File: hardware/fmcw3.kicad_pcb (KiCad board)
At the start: 4 copper layers, 101.8 x 46.8 mm, 430 parts, among them CON1 SD_Card_DM3BT, CON2 BARREL_JACK, P1 SMA, P10 CONN_01X01, P11 CONN_01X01, P12 CONN_01X01, P13 CONN_01X01, P14 CONN_01X01, P15 CONN_01X01, P16 CONN_01X01, P2 SMA, P3 CONN_02X04, P4 CONN_02X04, P5 CONN_01X01, P6 CONN_01X01, P7 CONN_01X01, P8 CONN_01X01, P9 CONN_01X01, Q1 RE1C002UN, Q2 DNP(RE1C002UN), SW1 DNP, SW2 SW_PUSH, U1 ADF4158, U10 HMC431LP4, U11 SKY65404, U12 PAT1220-6dB, U13 TRF37A73, U14 MGA-25203, U15 SMA, U16 SKY65404, U17 L7980, U18 L7980, U19 L7980, U2 LP5907-1.8, U20 LP5907-3.0, U21 LP2985A-10DBVR, U22 TPS7A91, U23 TPS7A91, U24 TPS7A91, U25 MIC5301-3.3, U26 5400BL15B050E, U27 5400BL15B050E, U28 5400BL15B050E, U29 ADL5802, U3 PAT1220-6dB, U30 XC7A15T-1FTG256C, U31 USB-MICRO, U32 93LC46B, U33 FT2232H, U34 ADA4940-2, U35 ADA4940-2, U39 LP5907-3.0, U4 KT2520K, U40 W25Q32JV, U5 NC7S04P5X, U6 NB3N551, U7 TLV172DCK, U8 LTC2292, U9 TRF37A73, Y1 ABM10-167-12.000MHZ-T3

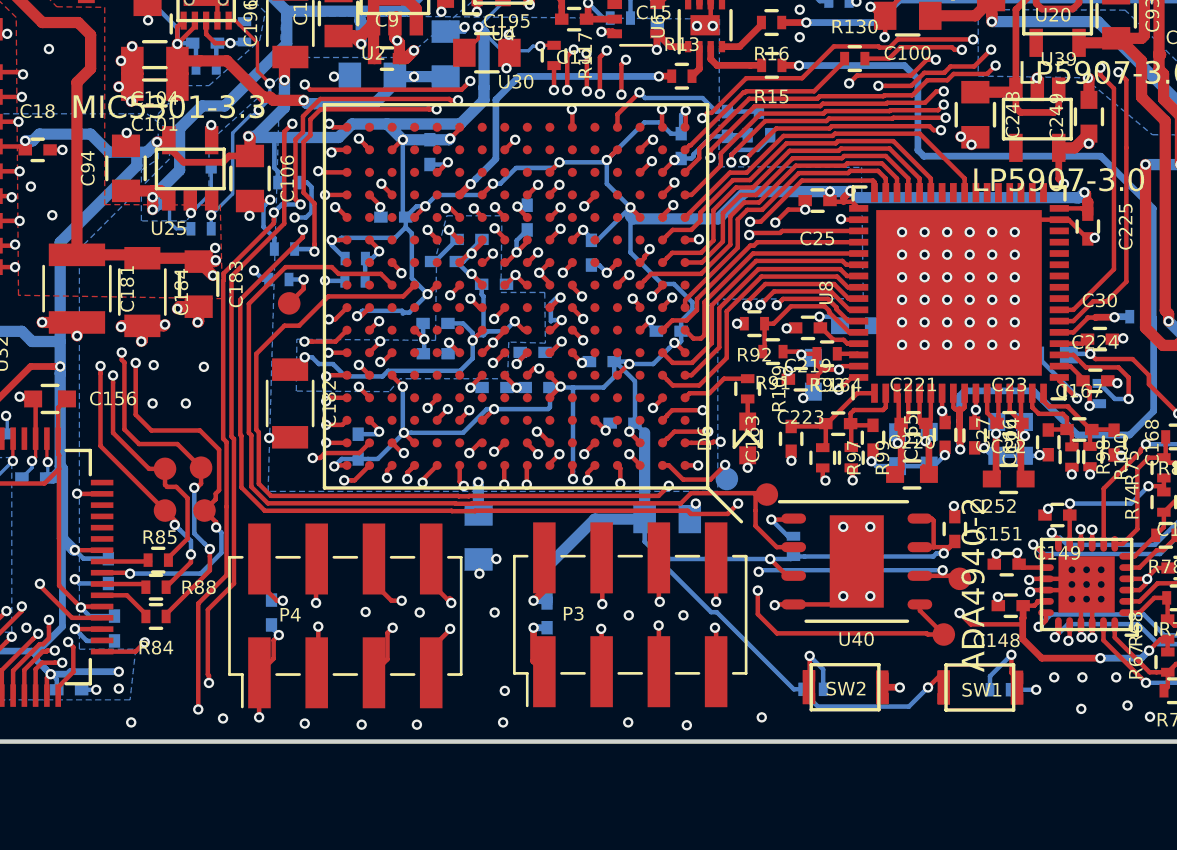
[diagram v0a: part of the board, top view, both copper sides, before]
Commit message: Fix FPGA programming resistor connections
M[2:0] were wired incorrectly when I ordered the board. For programming from SPI
memory M[2:0] should be "001", but I had them wired backwards as "100". I fixed
it with one jump wire, but here is a proper fix for anyone looking to reproduce
the design.
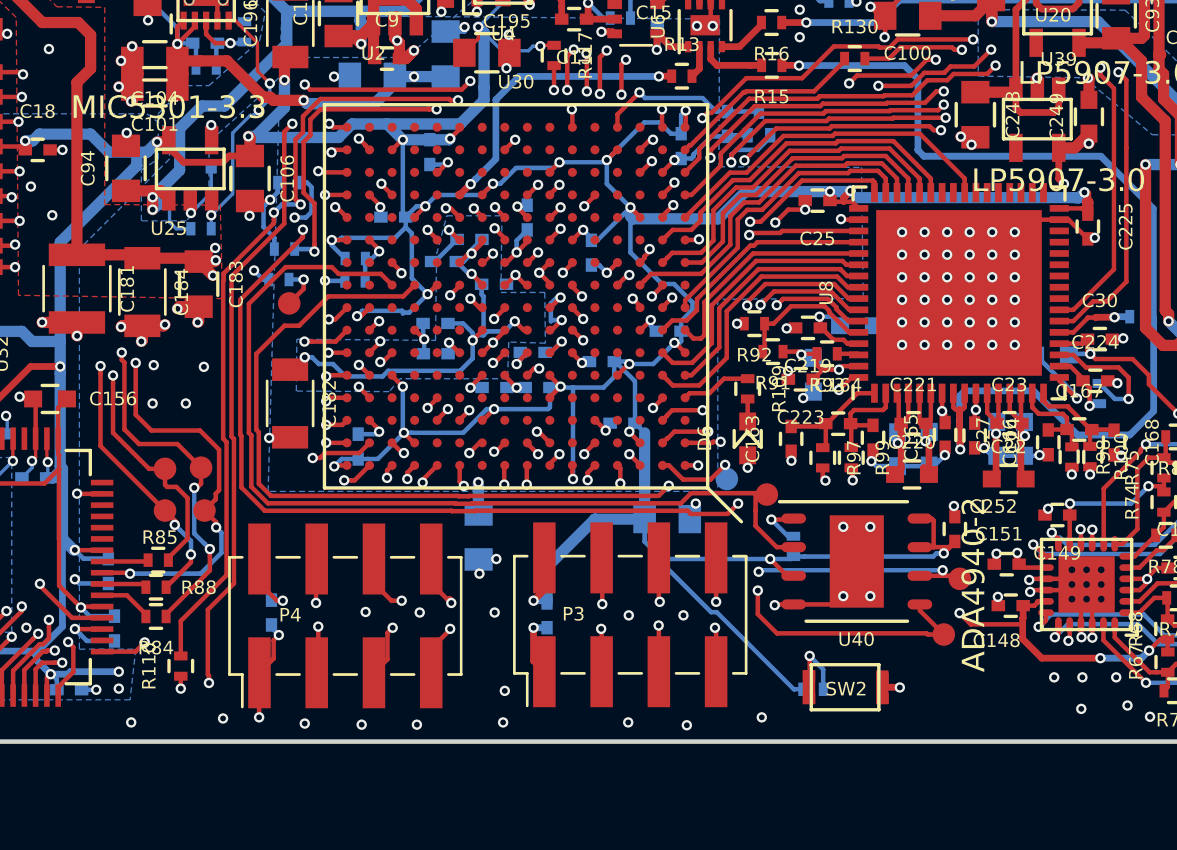
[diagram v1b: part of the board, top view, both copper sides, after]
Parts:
- removed SW1: DNP, fmcw3:EVP-AWBA2A
- C74: value 4.7n -> 8.2n
- R110: moved to F.Cu
- R115: value DNP -> 0
- R41: value 100 -> 56
- moved R110 36.4 mm to (146.0, 121.0), turned to 90 degrees
- turned R115 to 180 degrees
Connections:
- R110 pad 1: /fpga/M0 -> /3V3D
- R110 pad 2: GND -> /fpga/M0
- R115 pad 1: /3V3D -> /fpga/M2
- R115 pad 2: /fpga/M2 -> GND
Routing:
- net /fpga/M0: track 82.5 -> 40.3 mm, vias 6 -> 4
- net /3V3D: track 329.9 -> 321.3 mm
- net GND: track 555.7 -> 555.5 mm, vias 686 -> 685

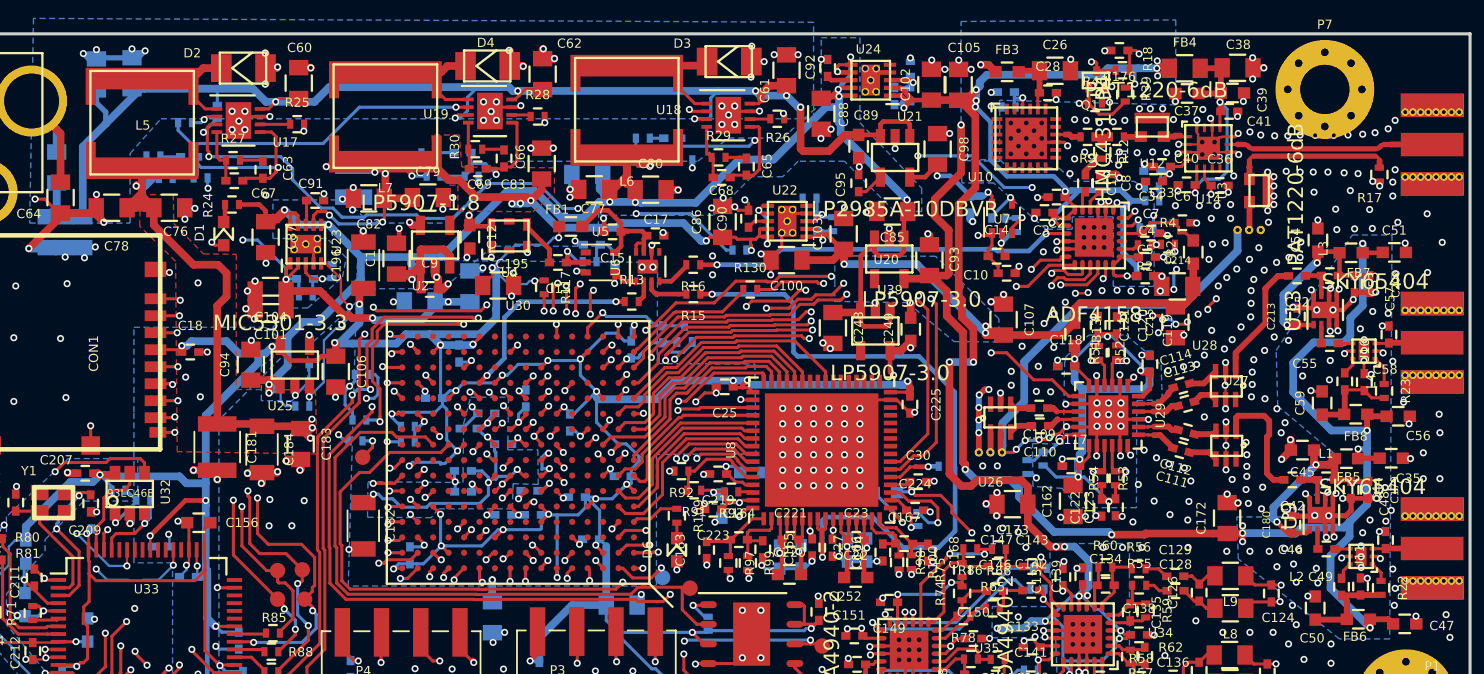
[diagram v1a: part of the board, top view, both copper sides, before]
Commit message: Update kicad:  * kicad_pcb from 20170123 to 20171130 (pcbnew from 75cda50 to 5ecfd32)  * EESchema from 2 to 4
fix pin 53 in U33 (remove path in pcb)
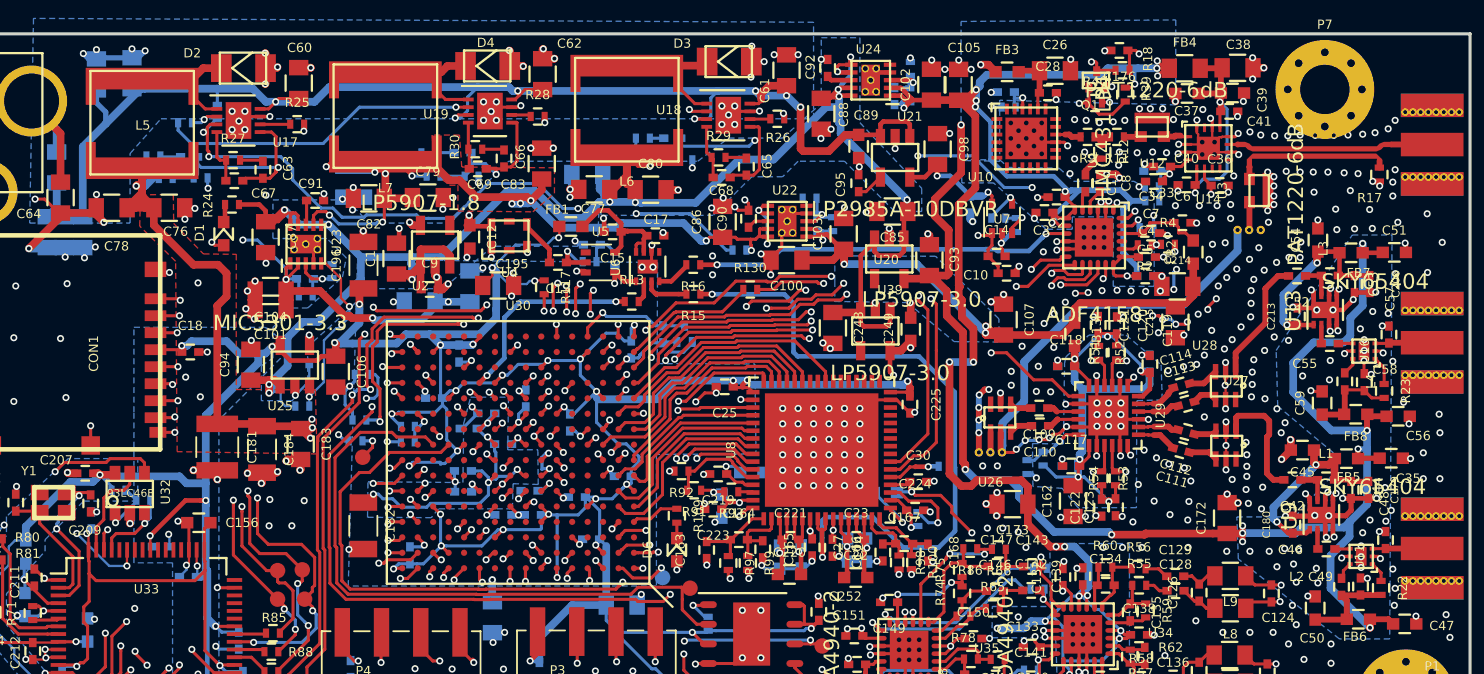
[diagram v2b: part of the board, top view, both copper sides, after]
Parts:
- C181: footprint Capacitors_SMD:C_1210 -> Capacitor_SMD:C_1210_3225Metric
- C182, C184, C196: footprint Capacitors_SMD:C_1206 -> Capacitor_SMD:C_1206_3216Metric
- CON2: value BARREL_JACK -> Barrel_Jack
- P10, P11, P12, P13, P14, P15, P16, P5, P6, P7, P8, P9: value CONN_01X01 -> Conn_01x01
- P3, P4: value CONN_02X04 -> Conn_02x04_Odd_Even; footprint Pin_Headers:Pin_Header_Straight_2x04_Pitch2.54mm_SMD -> Connector_PinHeader_2.54mm:PinHeader_2x04_P2.54mm_Vertical_SMD
- SW2: value SW_PUSH -> SW_Push
- U17, U18, U19: footprint Housings_DFN_QFN:DFN-8-1EP_3x3mm_Pitch0.5mm -> Package_DFN_QFN:DFN-8-1EP_3x3mm_P0.5mm_EP1.66x2.38mm
- U29: footprint Housings_DFN_QFN:QFN-24-1EP_4x4mm_Pitch0.5mm -> Package_DFN_QFN:QFN-24-1EP_4x4mm_P0.5mm_EP2.6x2.6mm
- U33: footprint Housings_QFP:LQFP-64_10x10mm_Pitch0.5mm -> Package_QFP:LQFP-64_10x10mm_P0.5mm
- U40: footprint Housings_DFN_QFN:DFN-S-8-1EP_6x5mm_Pitch1.27mm -> Package_DFN_QFN:DFN-S-8-1EP_6x5mm_P1.27mm
- U5, U7: footprint TO_SOT_Packages_SMD:SOT-353_SC-70-5 -> Package_TO_SOT_SMD:SOT-353_SC-70-5
- U8: footprint Housings_DFN_QFN:QFN-64-1EP_9x9mm_Pitch0.5mm -> Package_DFN_QFN:QFN-64-1EP_9x9mm_P0.5mm_EP7.35x7.35mm
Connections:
- net Net-(C15-Pad1) renamed VCC
- U1 pad 21: Net-(U1-Pad21) -> (no net)
- U22 pad 5: Net-(U22-Pad5) -> (no net)
- U24 pad 5: Net-(U24-Pad5) -> (no net)
- U30 pad A10: Net-(U30-PadA10) -> (no net)
- U30 pad B11: Net-(U30-PadB11) -> (no net)
- U30 pad B12: Net-(U30-PadB12) -> (no net)
- U30 pad B4: Net-(U30-PadB4) -> (no net)
- U30 pad B6: Net-(U30-PadB6) -> (no net)
- U30 pad C1: Net-(U30-PadC1) -> (no net)
- U30 pad C13: Net-(U30-PadC13) -> (no net)
- U30 pad C14: Net-(U30-PadC14) -> (no net)
- U30 pad C3: Net-(U30-PadC3) -> (no net)
- U30 pad C4: Net-(U30-PadC4) -> (no net)
- U30 pad C6: Net-(U30-PadC6) -> (no net)
- U30 pad C7: Net-(U30-PadC7) -> (no net)
- U30 pad C8: Net-(U30-PadC8) -> (no net)
- U30 pad C9: Net-(U30-PadC9) -> (no net)
- U30 pad D10: Net-(U30-PadD10) -> (no net)
- U30 pad D11: Net-(U30-PadD11) -> (no net)
- U30 pad D13: Net-(U30-PadD13) -> (no net)
- U30 pad D14: Net-(U30-PadD14) -> (no net)
- U30 pad D3: Net-(U30-PadD3) -> (no net)
- U30 pad D4: Net-(U30-PadD4) -> (no net)
- U30 pad D5: Net-(U30-PadD5) -> (no net)
- U30 pad D6: Net-(U30-PadD6) -> (no net)
- U30 pad D8: Net-(U30-PadD8) -> (no net)
- U30 pad D9: Net-(U30-PadD9) -> (no net)
- U30 pad E11: Net-(U30-PadE11) -> (no net)
- U30 pad E12: Net-(U30-PadE12) -> (no net)
- U30 pad E13: Net-(U30-PadE13) -> (no net)
- U30 pad E3: Net-(U30-PadE3) -> (no net)
- U30 pad E5: Net-(U30-PadE5) -> (no net)
- U30 pad E6: Net-(U30-PadE6) -> (no net)
- U30 pad F12: Net-(U30-PadF12) -> (no net)
- U30 pad F13: Net-(U30-PadF13) -> (no net)
- U30 pad F3: Net-(U30-PadF3) -> (no net)
- U30 pad F4: Net-(U30-PadF4) -> (no net)
- U30 pad F5: Net-(U30-PadF5) -> (no net)
- U30 pad G11: Net-(U30-PadG11) -> (no net)
- U30 pad G12: Net-(U30-PadG12) -> (no net)
- U30 pad G14: Net-(U30-PadG14) -> (no net)
- U30 pad G4: Net-(U30-PadG4) -> (no net)
- U30 pad G5: Net-(U30-PadG5) -> (no net)
- U30 pad H11: Net-(U30-PadH11) -> (no net)
- U30 pad H12: Net-(U30-PadH12) -> (no net)
- U30 pad H13: Net-(U30-PadH13) -> (no net)
- U30 pad H14: Net-(U30-PadH14) -> (no net)
- U30 pad H4: Net-(U30-PadH4) -> (no net)
- U30 pad H5: Net-(U30-PadH5) -> (no net)
- U30 pad H8: Net-(U30-PadH8) -> (no net)
- U30 pad J1: Net-(U30-PadJ1) -> (no net)
- U30 pad J15: Net-(U30-PadJ15) -> (no net)
- U30 pad J16: Net-(U30-PadJ16) -> (no net)
- U30 pad J5: Net-(U30-PadJ5) -> (no net)
- U30 pad K12: Net-(U30-PadK12) -> (no net)
- U30 pad K13: Net-(U30-PadK13) -> (no net)
- U30 pad K15: Net-(U30-PadK15) -> (no net)
- U30 pad K16: Net-(U30-PadK16) -> (no net)
- U30 pad K5: Net-(U30-PadK5) -> (no net)
- U30 pad L13: Net-(U30-PadL13) -> (no net)
- U30 pad L14: Net-(U30-PadL14) -> (no net)
- U30 pad L3: Net-(U30-PadL3) -> (no net)
- U30 pad L4: Net-(U30-PadL4) -> (no net)
- U30 pad L5: Net-(U30-PadL5) -> (no net)
- U30 pad M12: Net-(U30-PadM12) -> (no net)
- U30 pad M14: Net-(U30-PadM14) -> (no net)
- U30 pad M15: Net-(U30-PadM15) -> (no net)
- U30 pad M4: Net-(U30-PadM4) -> (no net)
- U30 pad M5: Net-(U30-PadM5) -> (no net)
- U30 pad M6: Net-(U30-PadM6) -> (no net)
- U30 pad N12: Net-(U30-PadN12) -> (no net)
- U30 pad N13: Net-(U30-PadN13) -> (no net)
- U30 pad N3: Net-(U30-PadN3) -> (no net)
- U30 pad N4: Net-(U30-PadN4) -> (no net)
- U30 pad N6: Net-(U30-PadN6) -> (no net)
- U30 pad N9: Net-(U30-PadN9) -> (no net)
- U30 pad P10: Net-(U30-PadP10) -> (no net)
- U30 pad P11: Net-(U30-PadP11) -> (no net)
- U30 pad P13: Net-(U30-PadP13) -> (no net)
- U30 pad P14: Net-(U30-PadP14) -> (no net)
- U30 pad P15: Net-(U30-PadP15) -> (no net)
- U30 pad P4: Net-(U30-PadP4) -> (no net)
- U30 pad P5: Net-(U30-PadP5) -> (no net)
- U30 pad P6: Net-(U30-PadP6) -> (no net)
- U30 pad P8: Net-(U30-PadP8) -> (no net)
- U30 pad P9: Net-(U30-PadP9) -> (no net)
- U30 pad R10: Net-(U30-PadR10) -> (no net)
- U30 pad R11: Net-(U30-PadR11) -> (no net)
- U30 pad R12: Net-(U30-PadR12) -> (no net)
- U30 pad R13: Net-(U30-PadR13) -> (no net)
- U30 pad R2: Net-(U30-PadR2) -> (no net)
- U30 pad R5: Net-(U30-PadR5) -> (no net)
- U30 pad R6: Net-(U30-PadR6) -> (no net)
- U30 pad R7: Net-(U30-PadR7) -> (no net)
- U30 pad R8: Net-(U30-PadR8) -> (no net)
- U30 pad T10: Net-(U30-PadT10) -> (no net)
- U30 pad T12: Net-(U30-PadT12) -> (no net)
- U30 pad T13: Net-(U30-PadT13) -> (no net)
- U30 pad T14: Net-(U30-PadT14) -> (no net)
- U30 pad T15: Net-(U30-PadT15) -> (no net)
- U30 pad T3: Net-(U30-PadT3) -> (no net)
- U30 pad T5: Net-(U30-PadT5) -> (no net)
- U30 pad T7: Net-(U30-PadT7) -> (no net)
- U30 pad T8: Net-(U30-PadT8) -> (no net)
- U30 pad T9: Net-(U30-PadT9) -> (no net)
- U31 pad 4: Net-(U31-Pad4) -> (no net)
- U31 pad SH: Net-(U31-PadSH) -> (no net)
- U33 pad 34: Net-(U33-Pad34) -> (no net)
- U33 pad 43: Net-(U33-Pad43) -> (no net)
- U33 pad 44: Net-(U33-Pad44) -> (no net)
- U33 pad 45: Net-(U33-Pad45) -> (no net)
- U33 pad 46: Net-(U33-Pad46) -> (no net)
- U33 pad 48: Net-(U33-Pad48) -> (no net)
- U33 pad 52: Net-(U33-Pad52) -> (no net)
- U33 pad 53: Net-(U33-Pad53) -> (no net)
- U33 pad 54: Net-(U33-Pad54) -> (no net)
- U33 pad 55: Net-(U33-Pad55) -> (no net)
- U33 pad 57: Net-(U33-Pad57) -> (no net)
- U33 pad 58: Net-(U33-Pad58) -> (no net)
- U33 pad 60: Net-(U33-Pad60) -> (no net)
- U6 pad 5: Net-(U6-Pad5) -> (no net)
- U8 pad 24: Net-(U8-Pad24) -> (no net)
- U8 pad 25: Net-(U8-Pad25) -> (no net)
- U8 pad 26: Net-(U8-Pad26) -> (no net)
- U8 pad 27: Net-(U8-Pad27) -> (no net)
- U8 pad 28: Net-(U8-Pad28) -> (no net)
- U8 pad 29: Net-(U8-Pad29) -> (no net)
- U8 pad 30: Net-(U8-Pad30) -> (no net)
- U8 pad 33: Net-(U8-Pad33) -> (no net)
- U8 pad 34: Net-(U8-Pad34) -> (no net)
- U8 pad 35: Net-(U8-Pad35) -> (no net)
- U8 pad 36: Net-(U8-Pad36) -> (no net)
- U8 pad 37: Net-(U8-Pad37) -> (no net)
- U8 pad 38: Net-(U8-Pad38) -> (no net)
- U8 pad 39: Net-(U8-Pad39) -> (no net)
- U8 pad 41: Net-(U8-Pad41) -> (no net)
- U8 pad 42: Net-(U8-Pad42) -> (no net)
- Y1 pad 2: Net-(Y1-Pad2) -> (no net)
- Y1 pad 4: Net-(Y1-Pad4) -> (no net)
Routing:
- net /fpga/usb/USB_5V: track 15.4 -> 4.30 mm, vias 2 -> 1
- net Net-(U33-Pad53): track 3.39 -> 0.00 mm, vias 1 -> 0
